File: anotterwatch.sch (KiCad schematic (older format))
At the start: 34 parts, among them J1 USB_C_Receptacle_USB2.0, Q1 Q_NMOS_GSD, Q2 nfet, Q3 npn, Q4 npn, U1 USBLC6-4SC6, U2 ESP32, U3 CH340C, U4 ST7789V

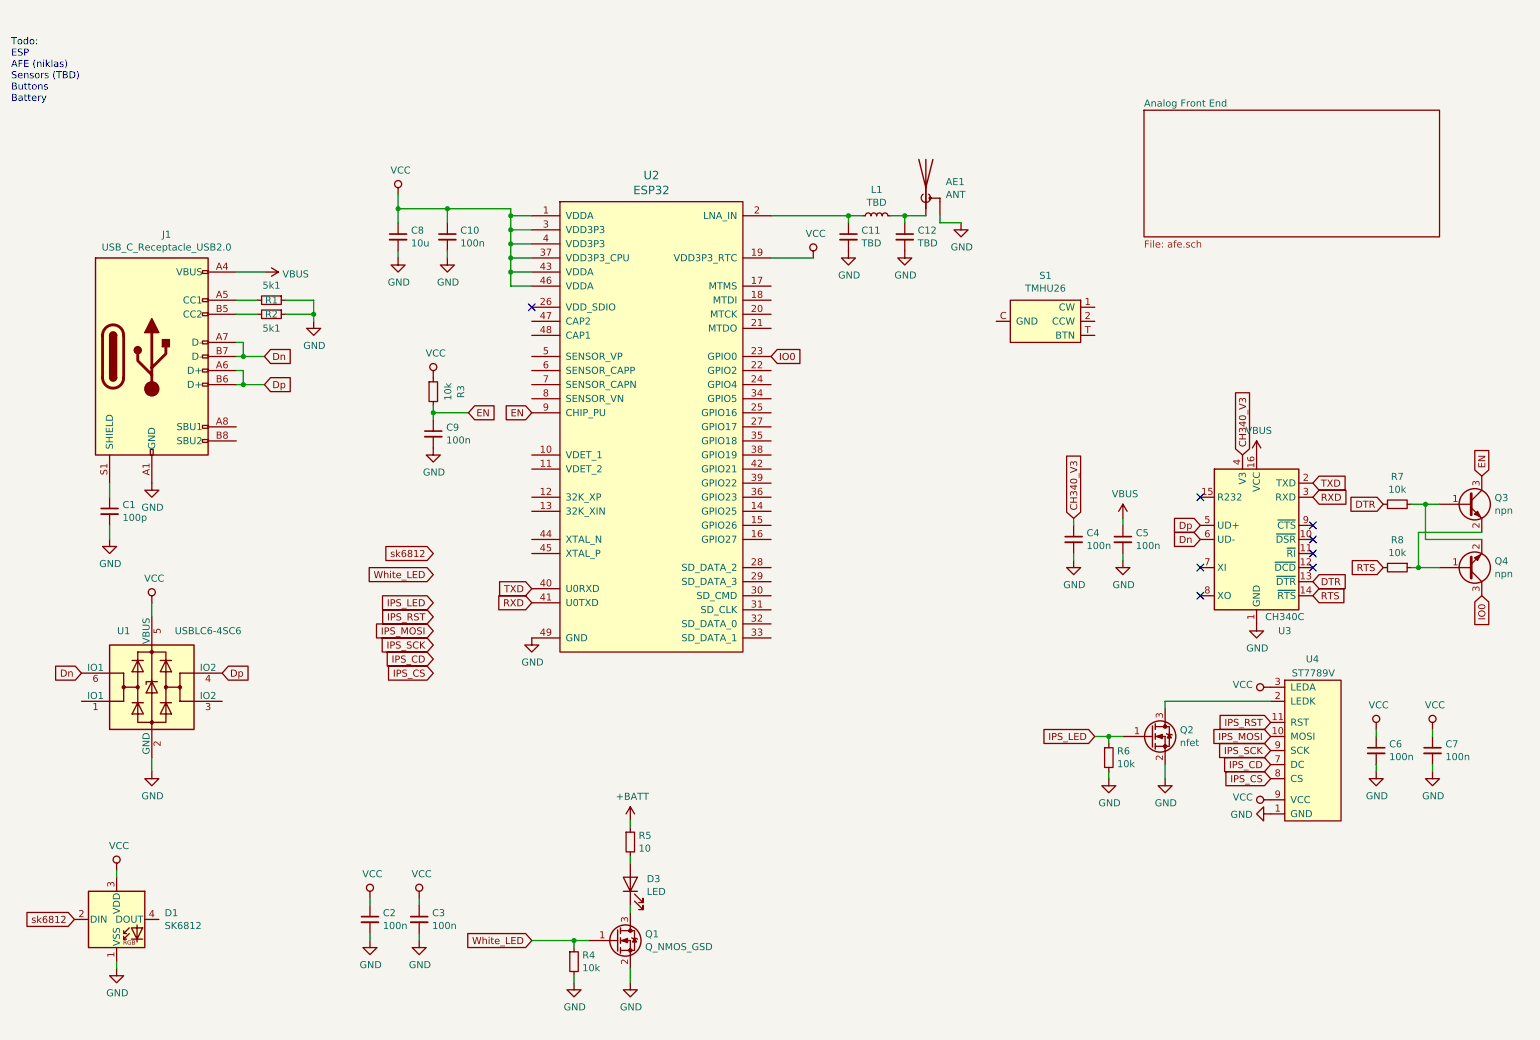
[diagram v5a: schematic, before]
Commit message: ADD: ESP32 pinout
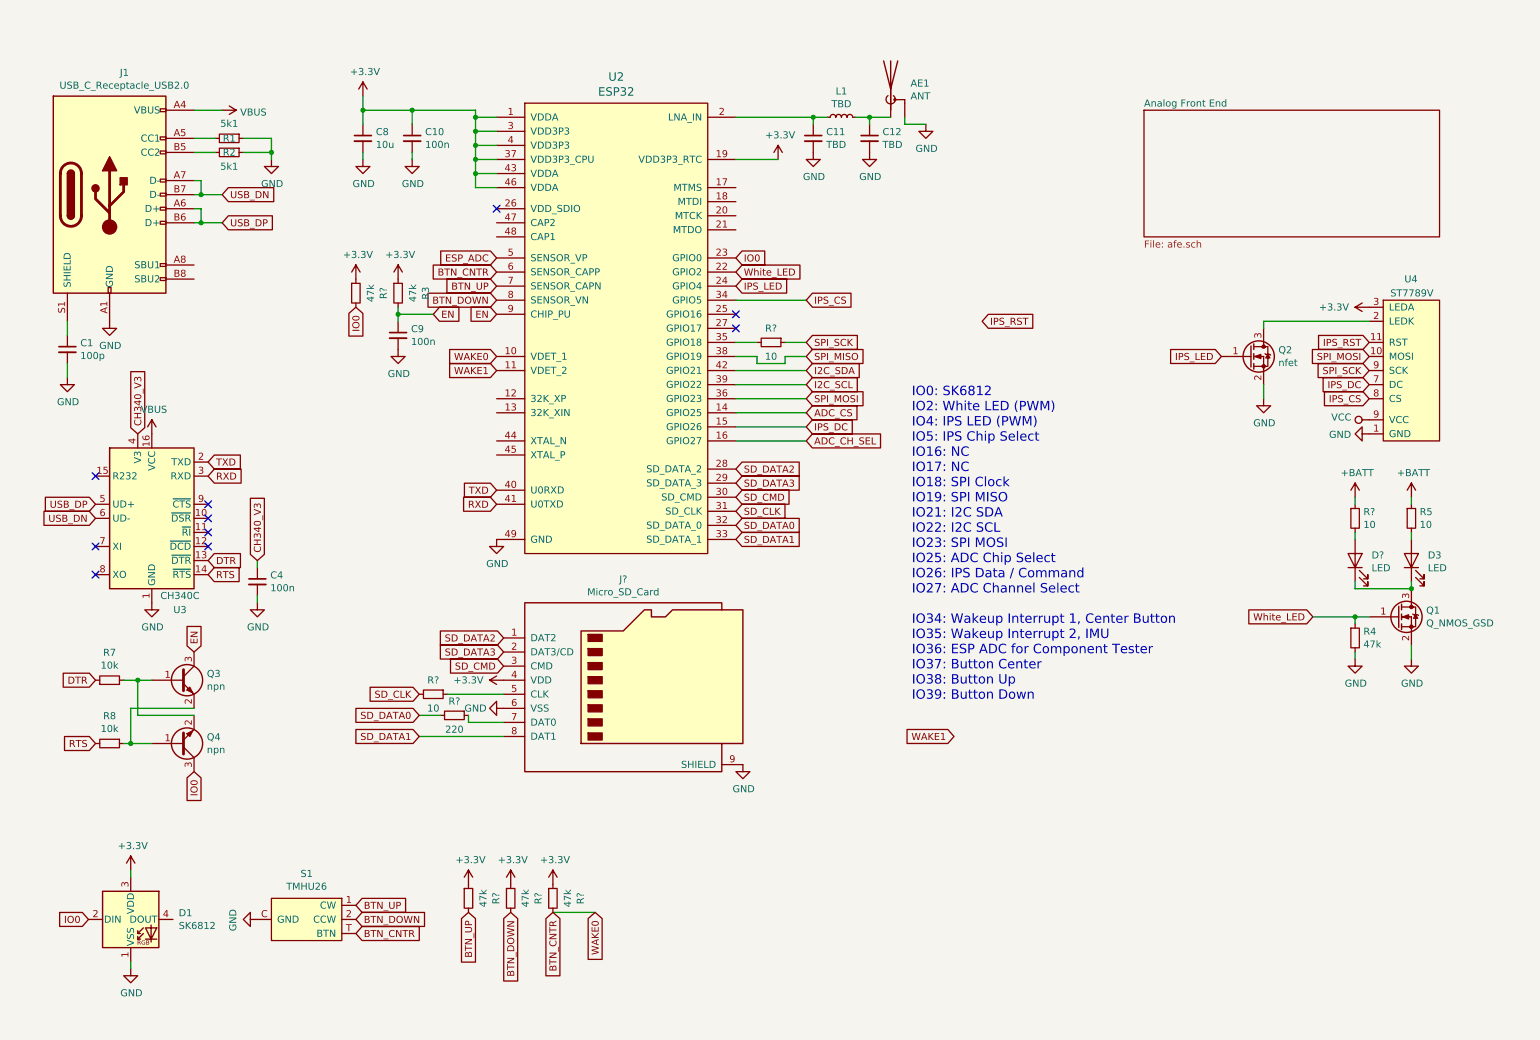
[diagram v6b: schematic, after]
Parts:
- removed C2, C3, C5, C6, C7: 100n, Capacitor_SMD:C_0603_1608Metric, symbol Device:C_Small
- removed R6: 10k, Resistor_SMD:R_0603_1608Metric, symbol Device:R_Small
- removed U1: USBLC6-4SC6, Package_TO_SOT_SMD:SOT-23-6, symbol Power_Protection:USBLC6-2SC6
- added D?: LED, LED_THT:LED_D5.0mm_Horizontal_O1.27mm_Z9.0mm, symbol Device:LED
- added J?: Micro_SD_Card, symbol Connector:Micro_SD_Card
- added R? (x2): 10, symbol Device:R_Small
- added R?: 220, symbol Device:R_Small
- added R? (x4): 47k, Resistor_SMD:R_0603_1608Metric, symbol Device:R_Small
- added R?: 10, Resistor_SMD:R_0603_1608Metric, symbol Device:R_Small
- R3, R4: value 10k -> 47k
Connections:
- net IPS_CD is gone; now on net IPS_DC: U4.7 (DC)
- net IPS_MOSI is gone; now on net SPI_MOSI: U4.10 (MOSI)
- net IPS_SCK is gone; now on net VCC: U4.9 (VCC)
- net sk6812 is gone; now on net IO0: D1.2 (DIN)
- net +BATT: now also R?.1
- net GND: now also S1.C (GND), J?.6 (VSS), J?.9 (SHIELD)
- net IO0: now also R?.2
- net IPS_CS: now also U2.34 (GPIO5)
- net IPS_LED: now also U2.24 (GPIO4)
- net VCC: no longer C10.1, C8.1, D1.3 (VDD), R3.1, U2.1 (VDDA), U2.19 (VDD3P3_RTC), U2.3 (VDD3P3), U2.37 (VDD3P3_CPU), U2.4 (VDD3P3), U2.43 (VDDA), U2.46 (VDDA), U4.3 (LEDA)
- net White_LED: now also U2.22 (GPIO2)
- net at D3.1 (K), Q1.3 (D): now also D?.1 (K)
- net BTN_CNTR: now reaches U2.10 (VDET_1)
- net BTN_CNTR: now also S1.T (BTN), U2.6 (SENSOR_CAPP), R?.2
- net WAKE1: now reaches U2.11 (VDET_2)
- net ADC_CS: now reaches U2.14 (GPIO25)
- net IPS_DC: now reaches U2.15 (GPIO26)
- net ADC_CH_SEL: now reaches U2.16 (GPIO27)
- net SD_DATA2: now reaches U2.28 (SD_DATA_2)
- net SD_DATA2: now also J?.1 (DAT2)
- net SD_DATA3: now reaches U2.29 (SD_DATA_3)
- net SD_DATA3: now also J?.2 (DAT3/CD)
- net SD_CMD: now reaches U2.30 (SD_CMD)
- net SD_CMD: now also J?.3 (CMD)
- net SD_CLK: now reaches U2.31 (SD_CLK)
- net SD_CLK: now also R?.2
- net SD_DATA0: now reaches U2.32 (SD_DATA_0)
- net SD_DATA0: now also R?.2
- net SD_DATA1: now reaches U2.33 (SD_DATA_1)
- net SD_DATA1: now also J?.8 (DAT1)
- net at U2.35 (GPIO18): now also R?.2
- net SPI_MOSI: now reaches U2.36 (GPIO23)
- net SPI_MISO: now reaches U2.38 (GPIO19)
- net I2C_SCL: now reaches U2.39 (GPIO22)
- net I2C_SDA: now reaches U2.42 (GPIO21)
- net ESP_ADC: now reaches U2.5 (SENSOR_VP)
- net BTN_UP: now reaches U2.7 (SENSOR_CAPN)
- net BTN_UP: now also S1.1 (CW), R?.2
- net BTN_DOWN: now reaches U2.8 (SENSOR_VN)
- net BTN_DOWN: now also S1.2 (CCW), R?.2
- net Dn renamed USB_DN
- net Dp renamed USB_DP
- new net: J?.5 (CLK), R?.1
- new net: J?.7 (DAT0), R?.1
- new net: D?.2 (A), R?.2
- new net +3V3: C10.1, C8.1, D1.3 (VDD), J?.4 (VDD), R3.1, R?.1, R?.1, R?.1, R?.1, U2.1 (VDDA), U2.19 (VDD3P3_RTC), U2.3 (VDD3P3), U2.37 (VDD3P3_CPU), U2.4 (VDD3P3), U2.43 (VDDA), U2.46 (VDDA), U4.3 (LEDA)
- new net SPI_SCK: R?.1, U4.9 (VCC)
- no-connect marks 8 -> 10
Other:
- note added: "IO0: SK6812\nIO2: White LED (PWM)\nIO4: IPS LED (PWM)\nIO5: IPS Chip Select\nIO16: NC\nIO17: NC\nIO18: SPI Clock\nIO19: SPI MISO\nIO21: I2C SDA\nIO22: I2C SCL\nIO23: SPI MOSI\nIO25: ADC Chip Select\nIO26: IPS Data / Command\nIO27: ADC Channel Select\n\nIO34: Wakeup Interrupt 1, Center Button\nIO35: Wakeup Interrupt 2, IMU\nIO36: ESP ADC for Component Tester\nIO37: Button Center\nIO38: Button Up\n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"
- note removed: "Todo: \nESP \nAFE (niklas) \nSensors (TBD)\nButtons\nBattery\n"
- moved on the sheet: AE1, C1, C10, C11, C12, C4, C8, C9, D1, D3, J1, L1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

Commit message: added BMI and TPS
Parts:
- added C2, C3: 100n, Capacitor_SMD:C_0603_1608Metric, symbol Device:C_Small
- added R36: 5k1, Resistor_SMD:R_0603_1608Metric, symbol Device:R_Small
- added U1: TP4056, symbol badgelib:TP4056
- added U12: BMI270, badgelib:BMI270, symbol badgelib:BMI270
- J1: symbol Connector:USB_C_Receptacle_USB2.0 -> anotterwatch-rescue:USB_C_Receptacle_USB2.0-Connector
- gave numbers to parts that had none: 10
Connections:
- net +BATT: now also C3.1, U1.5 (BAT)
- net GND: now also C2.2, C3.2, R36.2, U1.1 (TEMP), U1.3 (GND)
- net VBUS: now also C2.1, U1.4 (VCC), U1.8 (CE)
- net WAKE1: now also U12.4 (INT1)
- new net: R36.1, U1.2 (PROG)
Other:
- moved on the sheet: D1, R31, R33, R34, S1

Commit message: *white smoke*
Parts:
- removed D1: SK6812, badgelib:sk6812_side, symbol LED:SK6812
- removed Q2: nfet, Package_TO_SOT_SMD:SOT-23, symbol Device:Q_NMOS_GSD
- added C?: 100n, Capacitor_SMD:C_0603_1608Metric, symbol Device:C_Small
- added D? (x4): SK6812MINI, LED_SMD:LED_SK6812MINI_PLCC4_3.5x3.5mm_P1.75mm, symbol LED:SK6812MINI
- added Q? (x2): AO3400, Package_TO_SOT_SMD:SOT-23, symbol Device:Q_NMOS_GSD
- added R? (x5): 47k, Resistor_SMD:R_0603_1608Metric, symbol Device:R_Small
- added R? (x3): 5k1, Resistor_SMD:R_0603_1608Metric, symbol Device:R_Small
- Q1: value Q_NMOS_GSD -> AO3400
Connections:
- net +3V3: now also U12.12 (CSB), U12.5 (VDDIO), U12.8 (VDD), U4.4 (VCC), U4.9 (VCC), D?.4 (VDD), D?.4 (VDD), D?.4 (VDD), D?.4 (VDD), R?.1, R?.1, R?.1, R?.1, R?.1, R?.1, R?.2
- net ADC_CS: now also U2.34 (GPIO5); no longer U2.14 (GPIO25)
- net BTN_CNTR: no longer U2.6 (SENSOR_CAPP)
- net GND: now also U12.1 (SDO), U12.6 (GNDIO), U12.7 (GND), U4.8 (CS), C?.2, Q?.2 (S), Q?.2 (S), R?.2
- net I2C_SCL: now also U12.13 (SCX), R?.2
- net I2C_SDA: now also U12.14 (SDX), R?.1
- net IO0: now also D?.3 (DIN)
- net IPS_LED: now also U2.13 (32K_XIN), Q?.1 (G); no longer U2.24 (GPIO4)
- net IPS_RST: now also C?.1, R?.2
- net SD_CLK: now also U2.17 (MTMS); no longer U2.31 (SD_CLK)
- net SD_CMD: now also U2.21 (MTDO), R?.2; no longer U2.30 (SD_CMD)
- net SD_DATA0: now also U2.22 (GPIO2), R?.2; no longer U2.32 (SD_DATA_0)
- net SD_DATA1: now also U2.24 (GPIO4); no longer U2.33 (SD_DATA_1)
- net SD_DATA2: now also U2.18 (MTDI); no longer U2.28 (SD_DATA_2)
- net SD_DATA3: now also U2.20 (MTCK), R?.2; no longer U2.29 (SD_DATA_3)
- net WHITE_LED: now reaches U2.12 (32K_XP)
- net WHITE_LED: now also Q1.1 (G), R4.1
- net at U4.2 (LEDK): now also Q?.3 (D)
- net CHRG: now reaches U1.7 (\CHRG)
- net CHRG: now also U2.6 (SENSOR_CAPP), R?.2
- removed net IPS_CS: U2.34 (GPIO5), U4.8 (CS)
- net SPI_MISO renamed ADC_MISO
- net SPI_MOSI renamed IPS_MOSI
- net SPI_SCK renamed ADC_SCK
- removed net VCC: U4.4 (VCC), U4.9 (VCC)
- removed net White_LED: Q1.1 (G), R4.1, U2.22 (GPIO2)
- new net: D?.1 (DOUT), D?.3 (DIN) (x3)
- new net: D?.2 (VSS), D?.2 (VSS), D?.2 (VSS), D?.2 (VSS), Q?.3 (D)
- new net ESP32_DAC: U2.14 (GPIO25)
- new net PARTY_ENABLE: Q?.1 (G), R?.1
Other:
- note added: "IO0: SK6812\nIO2: SD Card SPI\nIO4: SD Card SPI\nIO5: ADC Chip Select\nIO16: NC\nIO17: NC\nIO18: ADC & IPS SPI Clock\nIO19: ADC SPI MISO\nIO21: I2C SDA\nIO22: I2C SCL\nIO23: IPS SPI MOSI\nIO25: DAC for """Self-Test"""\nIO26: IPS Data / Command\nIO27: ADC Channel Select\n\nIO32: White LED (PWM)\nIO33: IPS LED (PWM)\nIO34: Wakeup Interrupt 1, Center Button\nIO35: Wakeup Interrupt 2, IMU\nIO36: ESP 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"
- note removed: "IO0: SK6812\nIO2: White LED (PWM)\nIO4: IPS LED (PWM)\nIO5: IPS Chip Select\nIO16: NC\nIO17: NC\nIO18: SPI Clock\nIO19: SPI MISO\nIO21: I2C SDA\nIO22: I2C SCL\nIO23: SPI MOSI\nIO25: ADC Chip Select\nIO26: IPS Data / Command\nIO27: ADC Channel Select\n\nIO34: Wakeup Interrupt 1, Center Button\nIO35: Wakeup Interrupt 2, IMU\nIO36: ESP ADC for Component Tester\nIO37: Button Center\nIO38: Button Up\n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"
- moved on the sheet: AE1, C11, C12, C2, C4, D2, D3, J3, L1, Q1, Q3, Q4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
